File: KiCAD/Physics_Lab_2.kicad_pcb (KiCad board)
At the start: 2 copper layers, 58.5 x 57 mm, 13 parts, among them J1 USB_C, U1 MCP73871, U2 S2B-PH-K-S-GW

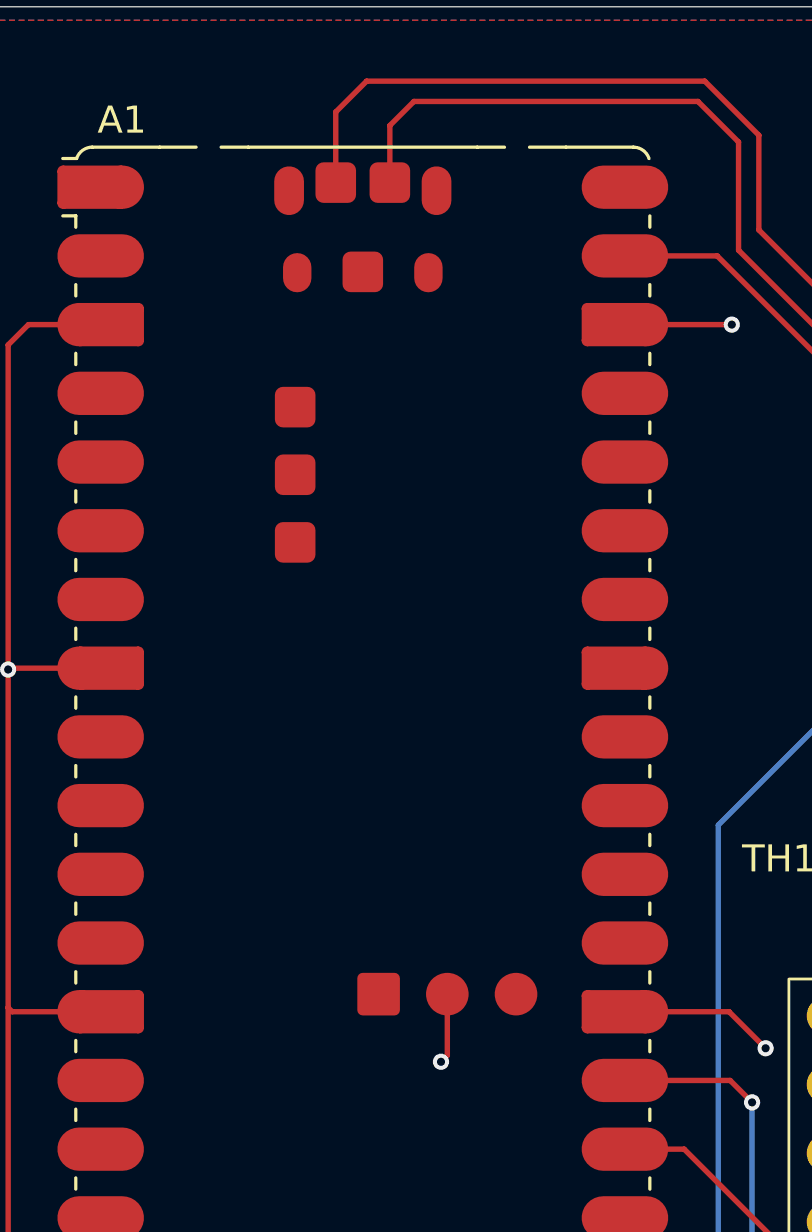
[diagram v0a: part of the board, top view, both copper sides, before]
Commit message: Remove TP1,4,5,6 and change TP2,3 to through hole
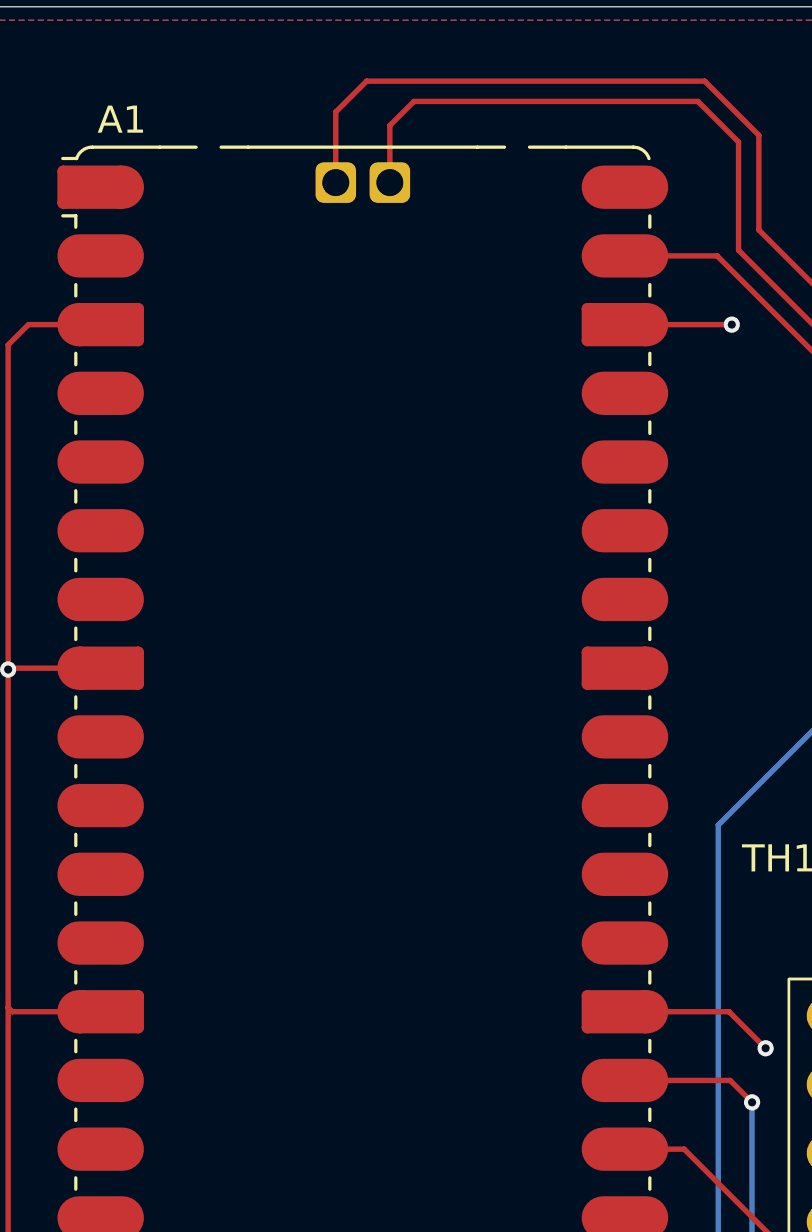
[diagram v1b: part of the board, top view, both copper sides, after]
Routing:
- net GND: track 114.0 -> 111.4 mm, vias 8 -> 7
